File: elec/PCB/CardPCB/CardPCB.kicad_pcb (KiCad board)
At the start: 2 copper layers, 88 x 50 mm, 22 parts, among them Q1 SL2312, Q2 SL2301S, SW1 SW_DPDT_x2, U1 LM555xM

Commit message: Final PCB
Generation of gerber and sending command
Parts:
- removed D1: TVS 5VWM 14VC SOD323, Diode_THT:D_DO-201AE_P15.24mm_Horizontal
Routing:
- net Net-(U1-THR): track 13.1 -> 23.5 mm

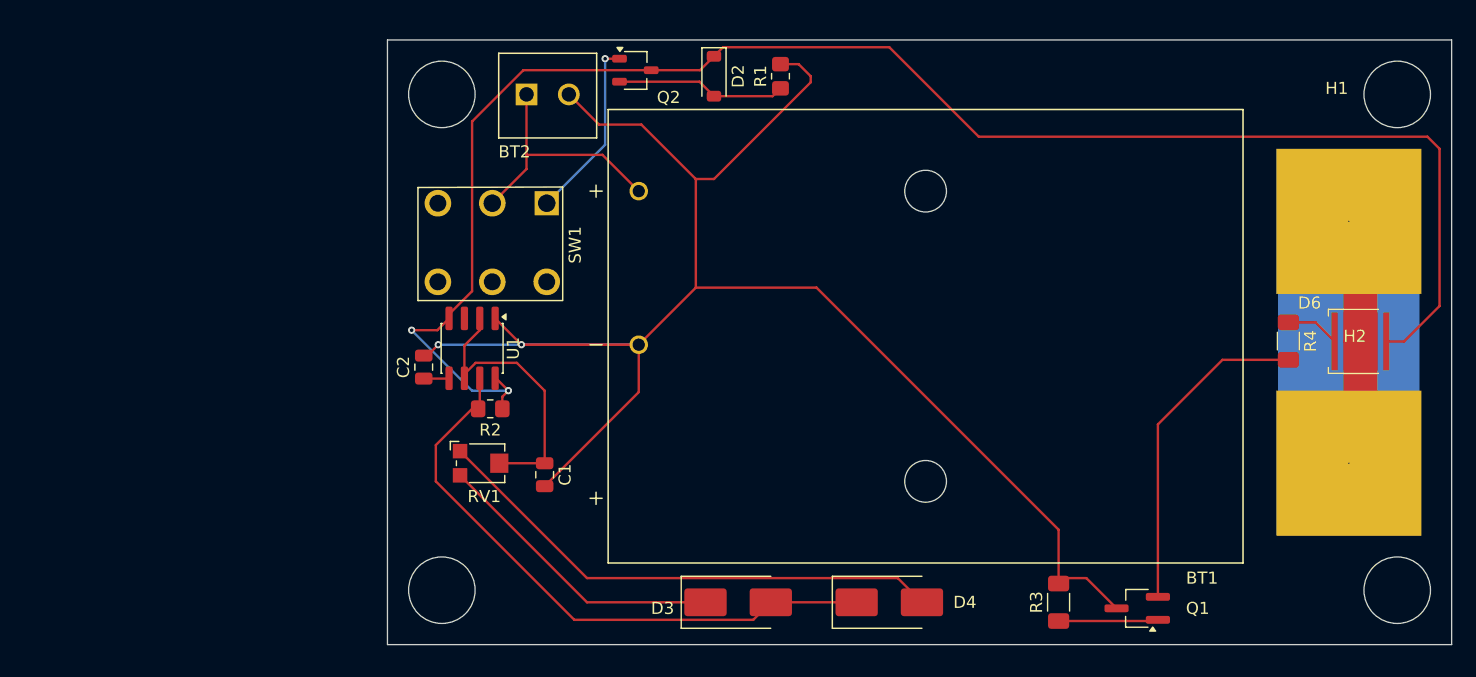
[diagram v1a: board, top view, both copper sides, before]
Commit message: Added digikey order
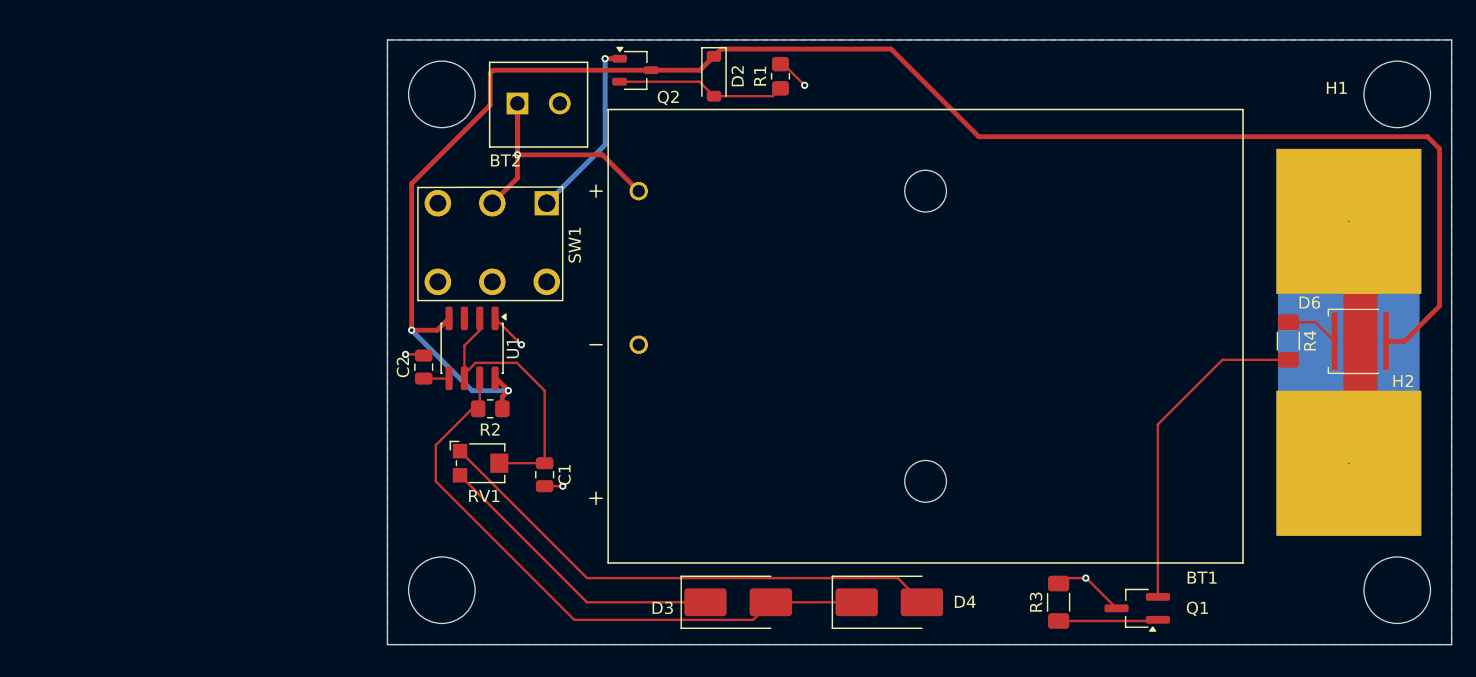
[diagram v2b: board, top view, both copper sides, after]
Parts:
- moved BT2 1.06 mm to (116.5, 62.2)
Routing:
- net -BATT: track 139.9 -> 14.9 mm, vias 2 -> 5
- net +BATT: track 20.7 -> 24.6 mm, vias 0 -> 1
- net VCC: track 139.6 -> 143.2 mm
- added copper zone on B.Cu, net -BATT
